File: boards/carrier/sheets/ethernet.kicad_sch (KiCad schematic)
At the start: 13 parts, among them J1 RJHSE5380, T1 HX5008NLT

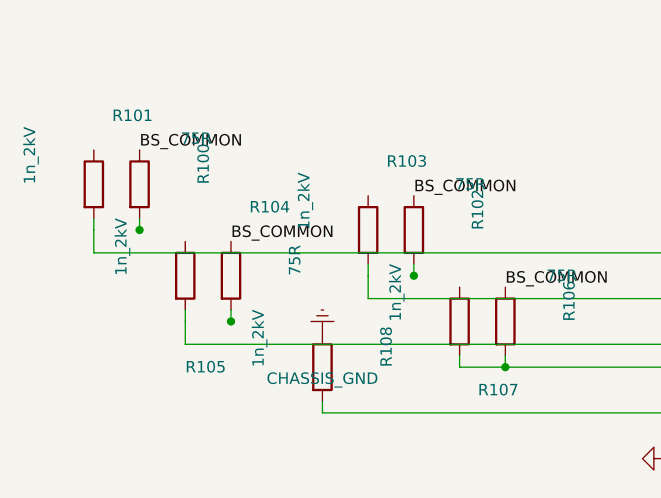
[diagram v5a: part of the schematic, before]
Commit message: planner: cluster drops start at ACTUAL trunk row (ERC 15→6)
When a cluster trunk takes a Z-bend (router picked an offset Y to
avoid an obstacle), the horizontal portion of the trunk isn't at
``pin_pos.y`` — it's at the offset Y the router chose. The drop
emitter was hardcoding ``drop_start = Point(slot_pos.x, pin_pos.y)``,
which sent the drop wire from a coordinate the trunk DOESN'T pass
through. The drop endpoint dangled and KiCad ERC fired
pin_not_connected on every affected cap's near pin (multiple per
cluster pin × multiple cluster pins per IC).

Fix: after the trunk is routed, walk the actual trunk segments and
pick the LONGEST horizontal (or vertical for TOP/BOTTOM) segment
that spans the slot's X (or Y). Use that segment's Y (or X) as the
drop's start coordinate. Falls back to ``pin_pos.y`` (or .x) when
no segment covers the slot (direct trunk case where this fallback
matches reality).

Closed all cap-near-pin pin_not_connected errors in usb_pd,
usbc_otg, and uart_bridge. ERC went from 15 → 6 errors.
Remaining 6 are:
  * ethernet R-pins (4) — magnetic-pair sub-slot pattern (no clean
    structural fix from the planner; needs a duplicate-label
    fallback that bypasses the strict label×label rule)
  * power_pin_not_driven (2) — microsd J1 VDD and ethernet PWR300
    (block configs don't supply a driver for these power nets)

Layout still 27/27 clean. 228 unit tests pass.

Co-Authored-By: Claude Opus 4.7 <noreply@anthropic.com>
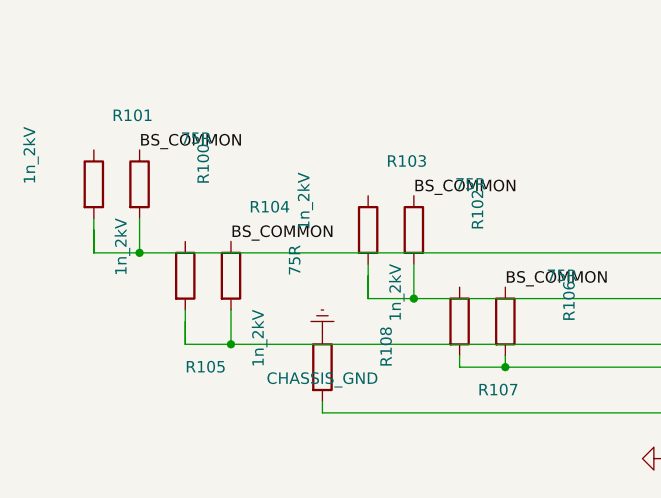
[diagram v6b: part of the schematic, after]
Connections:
- net at R102.2: now also R103.2, T1.10 (CT_PAIR1)
- net at R104.2: now also R105.2, T1.11 (CT_PAIR2)
- net at R101.2, T1.9 (CT_PAIR0): now also R100.2
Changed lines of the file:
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@@
 		(instances
 			(project "Ethernet (PHY MDI → HX5008 magnetics → RJ45)"
-				(path "/401515c4-7362-4cf0-8234-a3a2bcc9e14b"
+				(path "/bc2d1248-f8f2-41d9-a1a5-53fc68af1a45"
 					(reference "T1")
 					(unit 1)
@@
 		(instances
 			(project "Ethernet (PHY MDI → HX5008 magnetics → RJ45)"
-				(path "/401515c4-7362-4cf0-8234-a3a2bcc9e14b"
+				(path "/bc2d1248-f8f2-41d9-a1a5-53fc68af1a45"
 					(reference "J1")
 					(unit 1)
@@
 		(instances
 			(project "Ethernet (PHY MDI → HX5008 magnetics → RJ45)"
-				(path "/401515c4-7362-4cf0-8234-a3a2bcc9e14b"
+				(path "/bc2d1248-f8f2-41d9-a1a5-53fc68af1a45"
 					(reference "#PWR200")
 					(unit 1)
@@
 		(instances
 			(project "Ethernet (PHY MDI → HX5008 magnetics → RJ45)"
-				(path "/401515c4-7362-4cf0-8234-a3a2bcc9e14b"
+				(path "/bc2d1248-f8f2-41d9-a1a5-53fc68af1a45"
 					(reference "R100")
 					(unit 1)
@@
 		(instances
 			(project "Ethernet (PHY MDI → HX5008 magnetics → RJ45)"
-				(path "/401515c4-7362-4cf0-8234-a3a2bcc9e14b"
+				(path "/bc2d1248-f8f2-41d9-a1a5-53fc68af1a45"
 					(reference "R101")
 					(unit 1)
@@
 		(instances
 			(project "Ethernet (PHY MDI → HX5008 magnetics → RJ45)"
-				(path "/401515c4-7362-4cf0-8234-a3a2bcc9e14b"
+				(path "/bc2d1248-f8f2-41d9-a1a5-53fc68af1a45"
 					(reference "R102")
 					(unit 1)
@@
 		(instances
 			(project "Ethernet (PHY MDI → HX5008 magnetics → RJ45)"
-				(path "/401515c4-7362-4cf0-8234-a3a2bcc9e14b"
+				(path "/bc2d1248-f8f2-41d9-a1a5-53fc68af1a45"
 					(reference "R103")
 					(unit 1)
@@
 		(instances
 			(project "Ethernet (PHY MDI → HX5008 magnetics → RJ45)"
-				(path "/401515c4-7362-4cf0-8234-a3a2bcc9e14b"
+				(path "/bc2d1248-f8f2-41d9-a1a5-53fc68af1a45"
 					(reference "R104")
 					(unit 1)
@@
 		(instances
 			(project "Ethernet (PHY MDI → HX5008 magnetics → RJ45)"
-				(path "/401515c4-7362-4cf0-8234-a3a2bcc9e14b"
+				(path "/bc2d1248-f8f2-41d9-a1a5-53fc68af1a45"
 					(reference "R105")
 					(unit 1)
@@
 		(instances
 			(project "Ethernet (PHY MDI → HX5008 magnetics → RJ45)"
-				(path "/401515c4-7362-4cf0-8234-a3a2bcc9e14b"
+				(path "/bc2d1248-f8f2-41d9-a1a5-53fc68af1a45"
 					(reference "R106")
 					(unit 1)
@@
 		(instances
 			(project "Ethernet (PHY MDI → HX5008 magnetics → RJ45)"
-				(path "/401515c4-7362-4cf0-8234-a3a2bcc9e14b"
+				(path "/bc2d1248-f8f2-41d9-a1a5-53fc68af1a45"
 					(reference "R107")
 					(unit 1)
@@
 		(instances
 			(project "Ethernet (PHY MDI → HX5008 magnetics → RJ45)"
-				(path "/401515c4-7362-4cf0-8234-a3a2bcc9e14b"
+				(path "/bc2d1248-f8f2-41d9-a1a5-53fc68af1a45"
 					(reference "R108")
 					(unit 1)
@@
 		(instances
 			(project "Ethernet (PHY MDI → HX5008 magnetics → RJ45)"
-				(path "/401515c4-7362-4cf0-8234-a3a2bcc9e14b"
+				(path "/bc2d1248-f8f2-41d9-a1a5-53fc68af1a45"
 					(reference "#PWR300")
 					(unit 1)
@@
 		(instances
 			(project "Ethernet (PHY MDI → HX5008 magnetics → RJ45)"
-				(path "/401515c4-7362-4cf0-8234-a3a2bcc9e14b"
+				(path "/bc2d1248-f8f2-41d9-a1a5-53fc68af1a45"
 					(reference "R109")
 					(unit 1)
@@
 		(instances
 			(project "Ethernet (PHY MDI → HX5008 magnetics → RJ45)"
-				(path "/401515c4-7362-4cf0-8234-a3a2bcc9e14b"
+				(path "/bc2d1248-f8f2-41d9-a1a5-53fc68af1a45"
 					(reference "#PWR301")
 					(unit 1)
@@
 		(instances
 			(project "Ethernet (PHY MDI → HX5008 magnetics → RJ45)"
-				(path "/401515c4-7362-4cf0-8234-a3a2bcc9e14b"
+				(path "/bc2d1248-f8f2-41d9-a1a5-53fc68af1a45"
 					(reference "R110")
 					(unit 1)
@@
 		(instances
 			(project "Ethernet (PHY MDI → HX5008 magnetics → RJ45)"
-				(path "/401515c4-7362-4cf0-8234-a3a2bcc9e14b"
+				(path "/bc2d1248-f8f2-41d9-a1a5-53fc68af1a45"
 					(reference "#PWR302")
 					(unit 1)
@@
 	(wire
 		(pts
-			(xy 53.34 60.96) (xy 53.34 59.69)
-		)
-		(stroke
-			(width 0)
-			(type default)
-		)
-	)
-	(wire
-		(pts
-			(xy 48.26 60.96) (xy 48.26 59.69)
+			(xy 53.34 63.5) (xy 53.34 59.69)
+		)
+		(stroke
+			(width 0)
+			(type default)
+		)
+	)
+	(wire
+		(pts
+			(xy 48.26 63.5) (xy 48.26 59.69)
 		)
 		(stroke
@@
 	(wire
 		(pts
-			(xy 83.82 66.04) (xy 83.82 64.77)
-		)
-		(stroke
-			(width 0)
-			(type default)
-		)
-	)
-	(wire
-		(pts
-			(xy 78.74 66.04) (xy 78.74 64.77)
+			(xy 83.82 68.58) (xy 83.82 64.77)
+		)
+		(stroke
+			(width 0)
+			(type default)
+		)
+	)
+	(wire
+		(pts
+			(xy 78.74 68.58) (xy 78.74 64.77)
 		)
 		(stroke
@@
 	(wire
 		(pts
-			(xy 63.5 71.12) (xy 63.5 69.85)
-		)
-		(stroke
-			(width 0)
-			(type default)
-		)
-	)
-	(wire
-		(pts
-			(xy 58.42 71.12) (xy 58.42 69.85)
+			(xy 63.5 73.66) (xy 63.5 69.85)
+		)
+		(stroke
+			(width 0)
+			(type default)
+		)
+	)
+	(wire
+		(pts
+			(xy 58.42 73.66) (xy 58.42 69.85)
 		)
 		(stroke
@@
 	)
 	(junction
-		(at 53.34 60.96)
+		(at 53.34 63.5)
 		(diameter 0)
 		(color 0 0 0 0)
 	)
 	(junction
-		(at 83.82 66.04)
+		(at 83.82 68.58)
 		(diameter 0)
 		(color 0 0 0 0)
 	)
 	(junction
-		(at 63.5 71.12)
+		(at 63.5 73.66)
 		(diameter 0)
 		(color 0 0 0 0)
